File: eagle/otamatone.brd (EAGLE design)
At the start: 65 x 43.3 mm, 39 parts, among them IC1 TDA2822M, K1 MK20DX256VLH7, T1 MCP1825S, X1 MINI-USB

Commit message: Incremental updates to schematic and firmware
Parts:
- removed X1: MINI-USB, otamatone:TALL_BOI
- added SX1: PIN, t32_ref:PTH_39MIL
- added U$3: VERT_USB, otamatone:TALL_BOI
- added U$4: VERT_JACK, otamatone:AUDIOJACK
- G1: device t32_ref:HC49US -> otamatone:CRYS
- moved U$1 118.3 mm to (-59.0, -50.6)
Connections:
- new net VBAT: SX1.1, U$1.1
- net AGND: now also U$4.G, U$4.R
- net GND: now also G1.P$1, G1.P$4, U$3.5, U$3.CASE, U$3.CASE@2; no longer X1.5, X1.CASE, X1.CASE@2
- net N$16: now also U$3.3; no longer X1.3
- net N$17: now also U$3.2; no longer X1.2
- net N$19: now also U$3.4; no longer X1.4
- net N$5: now also G1.P$2; no longer G1.1
- net N$6: now also G1.P$3; no longer G1.2
- net N$7: now also U$4.L
- net VIN: now also U$1.0
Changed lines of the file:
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@@
 <?xml version="1.0" encoding="utf-8"?>
 <!DOCTYPE eagle SYSTEM "eagle.dtd">
-<eagle version="8.3.1">
+<eagle version="8.6.2">
 <drawing>
 <settings>
@@
 <param name="dpMaxLengthDifference" value="10mm"/>
 <param name="dpGapFactor" value="2.5"/>
-<param name="checkGrid" value="0"/>
 <param name="checkAngle" value="0"/>
 <param name="checkFont" value="1"/>
 <param name="checkRestrict" value="1"/>
+<param name="checkStop" value="0"/>
+<param name="checkValues" value="0"/>
 <param name="useDiameter" value="13"/>
 <param name="maxErrors" value="50"/>
@@
 <attribute name="TYPE" value="Capacitor" x="-15.24" y="46.99" size="1.778" layer="27" display="off"/>
 </element>
-<element name="G1" library="t32_ref" package="HC49US" value="16MHz" x="32.1056" y="38.481">
-<attribute name="DESC" value="16MHz / 18pF / 10ppm" x="32.1056" y="38.481" size="1.778" layer="27" display="off"/>
-<attribute name="MF" value="ABRACON" x="32.1056" y="38.481" size="1.778" layer="27" display="off"/>
-<attribute name="MPN" value="ABL-16.000MHz-B1U" x="32.1056" y="38.481" size="1.778" layer="27" display="off"/>
-<attribute name="OC_MOUSER" value="815-ABL-16-B1U" x="32.1056" y="38.481" size="1.778" layer="27" display="off"/>
-<attribute name="PACKAGE" value="HC-49US" x="32.1056" y="38.481" size="1.778" layer="27" display="off"/>
-<attribute name="TYPE" value="Crystal" x="32.1056" y="38.481" size="1.778" layer="27" display="off"/>
-</element>
+<element name="G1" library="otamatone" package="CRYS" value="16MHz" x="32.1056" y="38.481"/>
 <element name="IC1" library="TDA2822M" package="DIL8" value="TDA2822M" x="-45.72" y="6.35"/>
 <element name="K1" library="t32_ref" package="LQFP64-05" value="MK20DX256VLH7" x="54.5084" y="11.6078">
@@
 <attribute name="TYPE" value="Voltage regulator" x="-40.64" y="19.05" size="1.778" layer="27" display="off"/>
 </element>
-<element name="X1" library="otamatone" package="TALL_BOI" value="MINI-USB" x="36.0324" y="6.955" rot="R180"/>
-<element name="U$1" library="otamatone" package="5PIN_POT" value="P170S" x="32.385" y="24.511"/>
 <element name="U$2" library="otamatone" package="QFN16" value="MKL02Z32VFG4" x="54.7116" y="2.667" rot="R180"/>
+<element name="U$3" library="otamatone" package="TALL_BOI" value="VERT_USB" x="32.766" y="10.033"/>
+<element name="U$4" library="otamatone" package="AUDIOJACK" value="VERT_JACK" x="-64.3636" y="-19.8628"/>
+<element name="SX1" library="t32_ref" package="PTH_39MIL" value="PIN" x="-63.373" y="-34.1376"/>
+<element name="U$1" library="otamatone" package="5PIN_POT" value="P170S" x="-58.9534" y="-50.5968"/>
 </elements>
 <signals>
@@
 <contactref element="C10" pad="2"/>
 <contactref element="R4" pad="1"/>
-<contactref element="X1" pad="CASE"/>
-<contactref element="X1" pad="5"/>
 <contactref element="T1" pad="2"/>
 <contactref element="T1" pad="PAD"/>
@@
 <contactref element="C1" pad="2"/>
 <contactref element="SV1" pad="2"/>
-<contactref element="X1" pad="CASE@2"/>
 <contactref element="U$2" pad="2"/>
 <contactref element="U$2" pad="EXP"/>
+<contactref element="U$3" pad="CASE"/>
+<contactref element="U$3" pad="CASE@2"/>
+<contactref element="U$3" pad="5"/>
+<contactref element="G1" pad="P$4"/>
+<contactref element="G1" pad="P$1"/>
 <wire x1="57.7596" y1="5.6928" x2="60.4234" y2="14.859" width="0" layer="19" extent="1-1"/>
+<wire x1="56.1116" y1="2.417" x2="57.7596" y2="5.6928" width="0" layer="19" extent="1-1"/>
+<wire x1="54.7116" y1="2.667" x2="56.1116" y2="2.417" width="0" layer="19" extent="1-1"/>
 <wire x1="48.5934" y1="13.8684" x2="60.4234" y2="14.859" width="0" layer="19" extent="1-1"/>
-<wire x1="36.0324" y1="6.955" x2="48.5934" y2="13.8684" width="0" layer="19" extent="1-1"/>
-<wire x1="33.9824" y1="5.655" x2="36.0324" y2="6.955" width="0" layer="19" extent="1-1"/>
-<wire x1="28.7324" y1="6.955" x2="33.9824" y2="5.655" width="0" layer="19" extent="16-16"/>
-<wire x1="11.6078" y1="16.5354" x2="28.7324" y2="6.955" width="0" layer="19" extent="16-16"/>
+<wire x1="36.966" y1="9.033" x2="48.5934" y2="13.8684" width="0" layer="19" extent="1-1"/>
+<wire x1="34.366" y1="8.133" x2="36.966" y2="9.033" width="0" layer="19" extent="1-1"/>
+<wire x1="28.566" y1="9.033" x2="34.366" y2="8.133" width="0" layer="19" extent="1-1"/>
+<wire x1="11.6078" y1="16.5354" x2="28.566" y2="9.033" width="0" layer="19" extent="1-1"/>
+<wire x1="32.7056" y1="38.981" x2="48.5934" y2="13.8684" width="0" layer="19" extent="1-1"/>
+<wire x1="34.8256" y1="40.481" x2="32.7056" y2="38.981" width="0" layer="19" extent="1-1"/>
 <wire x1="-15.24" y1="35.814" x2="11.6078" y2="16.5354" width="0" layer="19" extent="1-1"/>
 <wire x1="-15.24" y1="46.228" x2="-15.24" y2="35.814" width="0" layer="19" extent="1-1"/>
@@
 <wire x1="-33.7312" y1="19.3294" x2="-40.64" y2="22.225" width="0" layer="19" extent="1-1"/>
 <wire x1="-27.2288" y1="19.3294" x2="-33.7312" y2="19.3294" width="0" layer="19" extent="1-1"/>
-<wire x1="54.7116" y1="2.667" x2="-40.64" y2="15.875" width="0" layer="19" extent="1-1"/>
-<wire x1="56.1116" y1="2.417" x2="54.7116" y2="2.667" width="0" layer="19" extent="1-1"/>
 </signal>
 <signal name="N$5">
 <contactref element="K1" pad="32"/>
-<contactref element="G1" pad="1"/>
+<contactref element="G1" pad="P$2"/>
 <contactref element="C10" pad="1"/>
-<wire x1="29.6926" y1="38.481" x2="-20.32" y2="47.752" width="0" layer="19" extent="1-1"/>
-<wire x1="58.2676" y1="5.6928" x2="29.6926" y2="38.481" width="0" layer="19" extent="1-1"/>
+<wire x1="34.7056" y1="38.981" x2="-20.32" y2="47.752" width="0" layer="19" extent="1-1"/>
+<wire x1="58.2676" y1="5.6928" x2="34.7056" y2="38.981" width="0" layer="19" extent="1-1"/>
 </signal>
 <signal name="N$6">
 <contactref element="K1" pad="33"/>
-<contactref element="G1" pad="2"/>
+<contactref element="G1" pad="P$3"/>
 <contactref element="C11" pad="1"/>
-<wire x1="34.5186" y1="38.481" x2="-25.4" y2="47.752" width="0" layer="19" extent="1-1"/>
-<wire x1="60.4234" y1="7.8486" x2="34.5186" y2="38.481" width="0" layer="19" extent="1-1"/>
+<wire x1="32.7056" y1="40.481" x2="-25.4" y2="47.752" width="0" layer="19" extent="1-1"/>
+<wire x1="60.4234" y1="7.8486" x2="32.7056" y2="40.481" width="0" layer="19" extent="1-1"/>
 </signal>
 <signal name="N$11">
@@
 <signal name="N$16">
 <contactref element="R6" pad="1"/>
-<contactref element="X1" pad="3"/>
-<wire x1="-41.91" y1="38.862" x2="32.3824" y2="5.655" width="0" layer="19" extent="1-1"/>
+<contactref element="U$3" pad="3"/>
+<wire x1="-41.91" y1="38.862" x2="32.766" y2="8.133" width="0" layer="19" extent="1-1"/>
 </signal>
 <signal name="N$17">
-<contactref element="X1" pad="2"/>
 <contactref element="R5" pad="1"/>
-<wire x1="-36.83" y1="38.862" x2="31.5824" y2="8.255" width="0" layer="19" extent="1-1"/>
+<contactref element="U$3" pad="2"/>
+<wire x1="-36.83" y1="38.862" x2="31.966" y2="10.033" width="0" layer="19" extent="1-1"/>
 </signal>
 <signal name="N$19">
-<contactref element="X1" pad="4"/>
 <contactref element="K1" pad="23"/>
 <contactref element="U$2" pad="6"/>
-<wire x1="33.1824" y1="8.255" x2="54.9616" y2="4.067" width="0" layer="19" extent="1-1"/>
-<wire x1="53.7464" y1="5.6928" x2="33.1824" y2="8.255" width="0" layer="19" extent="1-1"/>
+<contactref element="U$3" pad="4"/>
+<wire x1="53.7464" y1="5.6928" x2="33.566" y2="10.033" width="0" layer="19" extent="1-1"/>
+<wire x1="54.9616" y1="4.067" x2="53.7464" y2="5.6928" width="0" layer="19" extent="1-1"/>
 </signal>
 <signal name="SDA0">
@@
 <contactref element="T1" pad="1"/>
 <contactref element="C1" pad="1"/>
+<contactref element="U$1" pad="0"/>
+<wire x1="-42.926" y1="15.875" x2="-69.2534" y2="-50.5968" width="0" layer="19" extent="1-16"/>
 <wire x1="-30.48" y1="42.672" x2="-42.926" y2="15.875" width="0" layer="19" extent="1-1"/>
 <wire x1="-48.26" y1="46.99" x2="-30.48" y2="42.672" width="0" layer="19" extent="1-1"/>
@@
 <signal name="N$7">
 <contactref element="C13" pad="2"/>
+<contactref element="U$4" pad="L"/>
+<wire x1="-35.56" y1="46.228" x2="-67.8636" y2="-20.7628" width="0" layer="19" extent="1-1"/>
 </signal>
 <signal name="20/NECK">
@@
 <contactref element="C6" pad="2"/>
 <contactref element="R4" pad="2"/>
-<wire x1="48.5934" y1="7.8486" x2="48.5934" y2="8.3566" width="0" layer="19" extent="1-1"/>
-<wire x1="-43.6" y1="29.21" x2="48.5934" y2="8.3566" width="0" layer="19" extent="1-1"/>
+<contactref element="U$4" pad="G"/>
+<contactref element="U$4" pad="R"/>
+<wire x1="-63.4636" y1="-15.4628" x2="-63.4636" y2="-23.1628" width="0" layer="19" extent="1-1"/>
+<wire x1="-43.6" y1="29.21" x2="-63.4636" y2="-15.4628" width="0" layer="19" extent="1-1"/>
 <wire x1="-45.72" y1="41.148" x2="-43.6" y2="29.21" width="0" layer="19" extent="1-1"/>
 <wire x1="-43.688" y1="45.72" x2="-45.72" y2="41.148" width="0" layer="19" extent="1-1"/>
@@
 <wire x1="-26.67" y1="38.862" x2="-43.688" y2="45.72" width="0" layer="19" extent="1-1"/>
 <wire x1="-21.59" y1="35.814" x2="-26.67" y2="38.862" width="0" layer="19" extent="1-1"/>
+<wire x1="48.5934" y1="8.3566" x2="-21.59" y2="35.814" width="0" layer="19" extent="1-1"/>
+<wire x1="48.5934" y1="7.8486" x2="48.5934" y2="8.3566" width="0" layer="19" extent="1-1"/>
 </signal>
 <signal name="N$8">
@@
 <wire x1="54.7624" y1="5.6928" x2="54.4616" y2="4.067" width="0" layer="19" extent="1-1"/>
 </signal>
+<signal name="VBAT">
+<contactref element="SX1" pad="1"/>
+<contactref element="U$1" pad="1"/>
+<wire x1="-63.373" y1="-34.1376" x2="-48.6534" y2="-50.5968" width="0" layer="19" extent="16-16"/>
+</signal>
 </signals>

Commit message: Updated schematics
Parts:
- removed C12: 0.1uF, t32_ref:C0603
- removed P1: (no value), t32_ref:LED-0805
- removed SX10, SX4, SX52, SX9: PIN, t32_ref:PTH_39MIL
- removed T1: MCP1825S, t32_ref:SOT-223
- added BTN_GND, S+, SX3, SX5: PINSMT, otamatone:SMD
- added BTN_GND1, BTN_GND2: PIN, t32_ref:PTH_39MIL
- added C15, C3: 10uF, rcl:C0603
- added C16, C17: 0.1uF, rcl:C0603
- added C18: 10nF, rcl:C0603
- added C19: 0.1uF, otamatone:C0402
- added C20: 2.2uF, otamatone:C0603
- added LED1: TLLR4400, led:LED3MM
- added R11: 10K, rcl:R0603
- added R12, R13: 4.7, rcl:R0603
- added R14, R15: 10K, rcl:R0402
- added U$5: LP38691, otamatone:SON65P210X210X80-7N
- C1: value 0.1uF -> 2.2uF; device t32_ref:C0603 -> otamatone:C0603
- C10, C11, C4, C5, C7, C8, C9: device t32_ref:C0603 -> otamatone:C0402
- C14: device rcl:C0603 -> rcl:C0402
- C2, C6: device t32_ref:C0805 -> otamatone:C0603
- IC1: value TDA2822M -> TDA2822MSOP8; device TDA2822M:DIL8 -> TDA2822M:SOP8
- R1, R10, R9: device t32_ref:R0603 -> rcl:R0402
- R2, R4: device t32_ref:L0603 -> otamatone:L0603
- R3, R5, R6: device t32_ref:R0603 -> otamatone:R0402
- R7: device t32_ref:SOT-23 -> otamatone:SOT-23
- R8: value 470R -> (none); device t32_ref:R0603 -> rcl:R0603
- S1: value (none) -> MOMENTARY-SWITCH-SPST-SMD-4.5MM; device t32_ref:ALPS_SKHH -> SparkFun-Switches:TACTILE_SWITCH_SMD_4.5MM
- SX2, SX8: value PIN -> PINSMT; device t32_ref:PTH_39MIL -> otamatone:SMD
- moved SX1 129.0 mm to (60.5, 2.18), flipped to the bottom
- moved U$4 121.5 mm to (53.6, 9.25)
- moved IC1 120.5 mm to (68.8, 43.9), flipped to the bottom, turned to 270 degrees
- moved U$1 118.3 mm to (32.4, 24.5), turned to 180 degrees
- moved C13 90.6 mm to (48.1, 12.1), flipped to the bottom
- moved K1 71.7 mm to (-16.6, 20.8), flipped to the bottom
- moved U$2 71.2 mm to (-16.1, 10.0), flipped to the bottom
- moved G1 63.9 mm to (-28.2, 17.3), flipped to the bottom, turned to 270 degrees
- moved C14 55.6 mm to (8.79, 45.2), turned to 270 degrees
- moved C1 54.0 mm to (20.0, 61.0)
- moved C2 47.8 mm to (26.0, 61.0), turned to 180 degrees
- moved S1 46.9 mm to (14.5, 8.00)
- moved R8 45.8 mm to (-1.19, 39.9)
- moved R4 44.6 mm to (-8.97, 18.7), flipped to the bottom, turned to 90 degrees
- moved SX2 44.0 mm to (-4.60, 41.7)
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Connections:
- removed net N$4: C13.1
- removed net N$54: K1.18, SX52.1
- new net FULLVOL: K1.18, U$1.4
- new net LBUTTON: K1.44, R14.1, SX5.P$1
- new net N$18: C16.1, R12.1
- new net N$21: C17.1, R13.1
- new net N$22: C15.2, C18.1, IC1.5
- new net RBUTTON: K1.63, R15.1, SX2.P$1
- new net S+: IC1.1, R12.2, S+.P$1
- new net S-: IC1.3, R13.2, SX3.P$1
- new net SOUND: C13.2, IC1.7, R11.2, U$4.L
- new net VOL_OUT: C13.1, U$1.3
- net 20/NECK: now also SX8.P$1; no longer SX8.1
- net AGND: now also C16.2, C17.2, C18.2, C3.2, IC1.4, IC1.6, R11.1, U$1.2
- net GND: now also BTN_GND.P$1, BTN_GND2.1, C19.2, C20.2, R14.2, R15.2, S1.2, U$5.2, U$5.7; no longer C12.2, S1.4, T1.2, T1.PAD
- net N$31: now also LED1.A; no longer P1.+
- net N$52: now also LED1.K; no longer P1.-
- net N$7: now also C15.1, IC1.8; no longer C13.2, U$4.L
- net N$9: now also S1.4; no longer S1.2
- net SCL0: no longer SX9.1
- net SDA0: no longer SX10.1
- net VCC: now also BTN_GND1.1, C19.1, C20.1, C3.1, IC1.2, U$5.4, U$5.5; no longer C12.1, SV1.1, SX4.1, T1.3
- net VIN: now also SV1.1, U$5.1, U$5.6; no longer SX2.1, T1.1
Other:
- outline, holes or cut-outs redrawn

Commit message: sync changes
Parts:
- removed R7: (no value), otamatone:SOT-23
- added U$6, U$7: SCHOTTKY, otamatone:LED-0805
- C9: value 0.1uF -> 2.2uF; device otamatone:C0402 -> otamatone:C0603
- U$5: value LP38691 -> AP2112K; device otamatone:SON65P210X210X80-7N -> otamatone:SOT25
- moved U$5 42.7 mm to (11.0, 20.0)
- moved LED1 35.0 mm to (32.2, 39.7)
- moved C9 20.3 mm to (10.0, 26.0), flipped to the top
- renumbered SX3 to S-
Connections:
- removed net N$68: C9.1, K1.21, R7.3
- new net N$1: U$1.1, U$6.-, U$7.-
- new net VUSB: C9.1, U$3.1, U$6.+
- net GND: no longer U$5.7
- net VBAT: now also U$7.+; no longer U$1.1
- net VCC: now also K1.21; no longer R7.1, U$5.4
- net VIN: now also U$5.3; no longer U$5.6

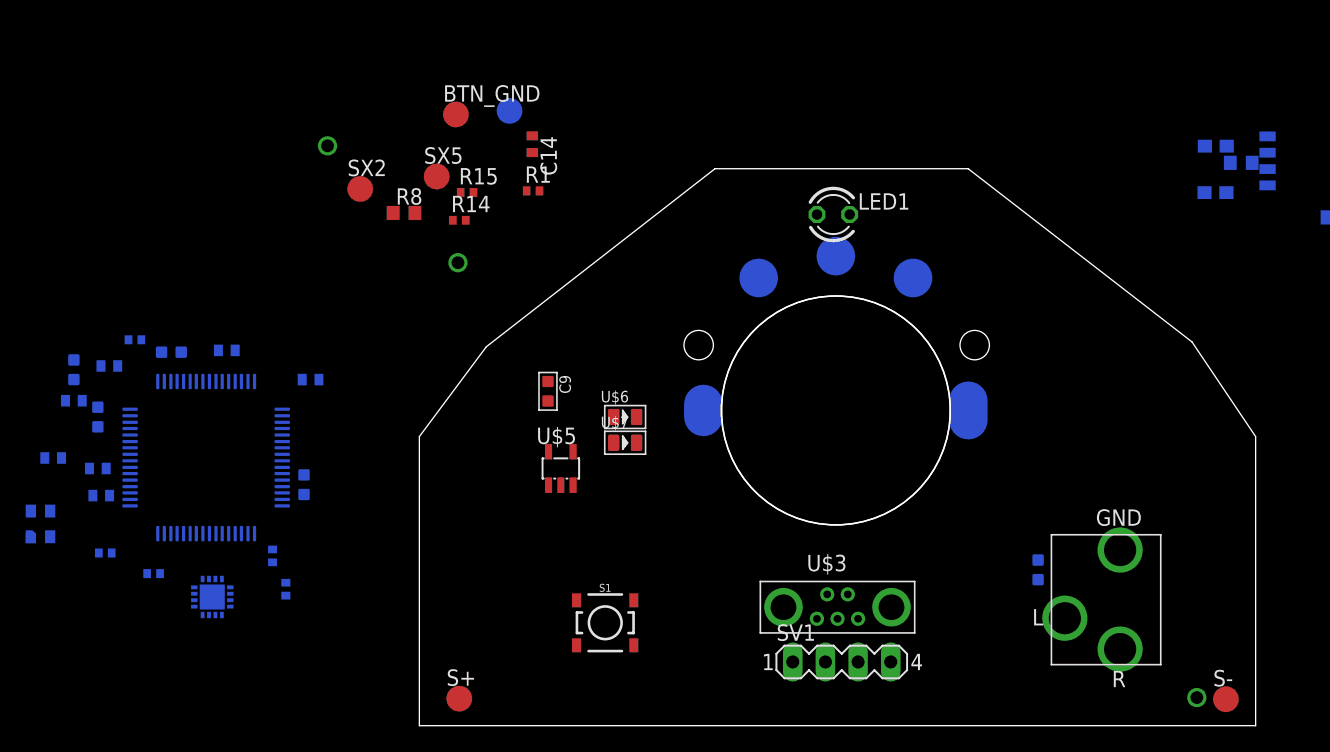
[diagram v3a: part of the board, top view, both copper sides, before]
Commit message: Updated gitignore and board contents
unrouted components are now drc compliant, through hole components have been place
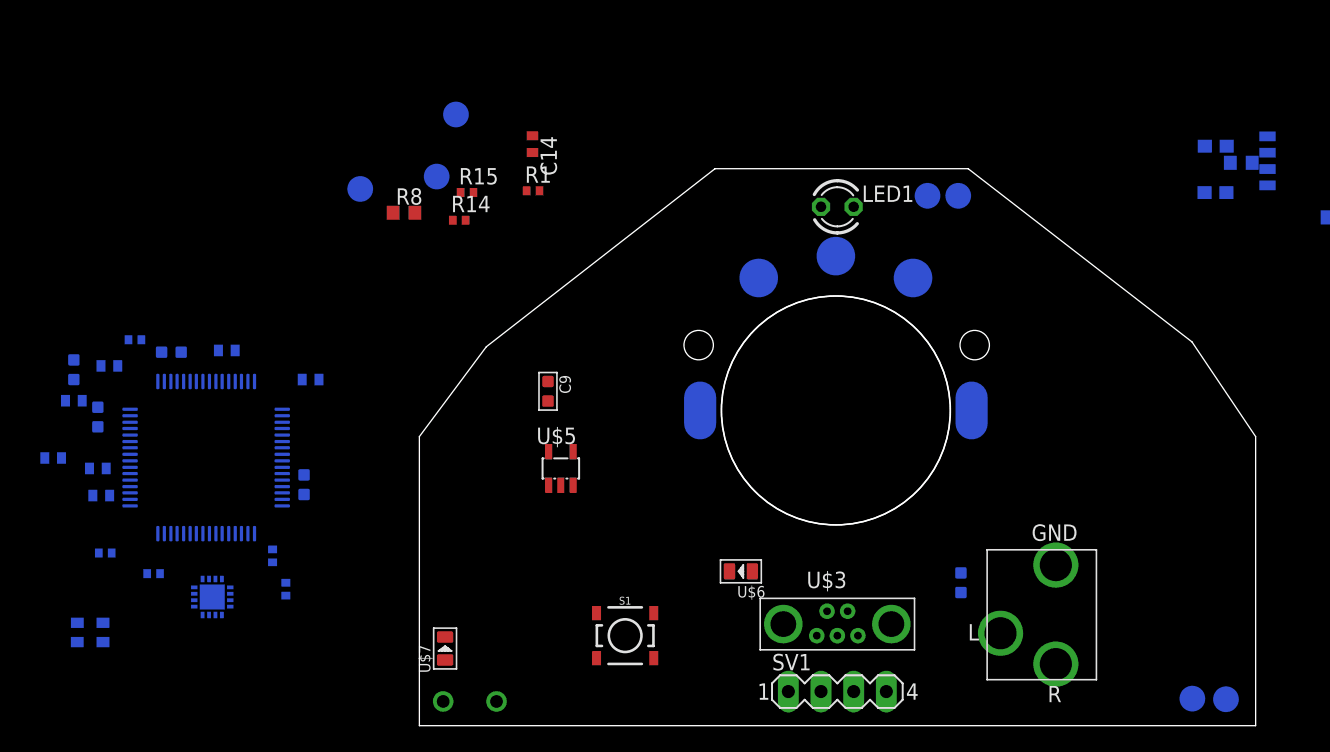
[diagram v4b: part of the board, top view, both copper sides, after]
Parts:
- removed BTN_GND1, BTN_GND2, SX1: PIN, t32_ref:PTH_39MIL
- removed SX8: PINSMT, otamatone:SMD
- added B+, B-: PIN, t32_ref:PTH_39MIL
- added Z+, Z-: PINSMT, otamatone:SMD
- G1: value 16MHz -> (none)
- moved S+ 57.0 mm to (60.1, 2.10), flipped to the bottom
- moved U$7 21.3 mm to (2.00, 6.00), turned to 90 degrees
- moved U$6 15.0 mm to (25.0, 12.0), turned to 180 degrees
- moved G1 12.0 mm to (-24.0, 6.00), turned to 0 degrees
- moved C13 6.08 mm to (42.1, 11.1)
- moved U$4 5.14 mm to (48.6, 8.08)
- moved SV1 2.33 mm to (32.5, 2.65)
- moved S1 1.84 mm to (16.0, 7.00)
- moved U$3 1.31 mm to (32.5, 8.90)
- moved LED1 0.68 mm to (32.5, 40.3)
- flipped BTN_GND to the bottom
- flipped S- to the bottom
- flipped SX2 to the bottom
- flipped SX5 to the bottom
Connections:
- net 20/NECK: now also Z-.P$1; no longer SX8.P$1
- net GND: now also B-.1; no longer BTN_GND2.1
- net VBAT: now also B+.1; no longer SX1.1
- net VCC: now also Z+.P$1; no longer BTN_GND1.1
